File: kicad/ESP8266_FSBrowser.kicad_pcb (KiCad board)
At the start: 2 copper layers, 28 parts, among them P1 POWER, P2 GPIO, P3 SERIAL, SW1 RESET, SW2 AP_ENABLE, SW3 FLASH, U1 ESP-12E, U2 SPX3819M5-L-3-3

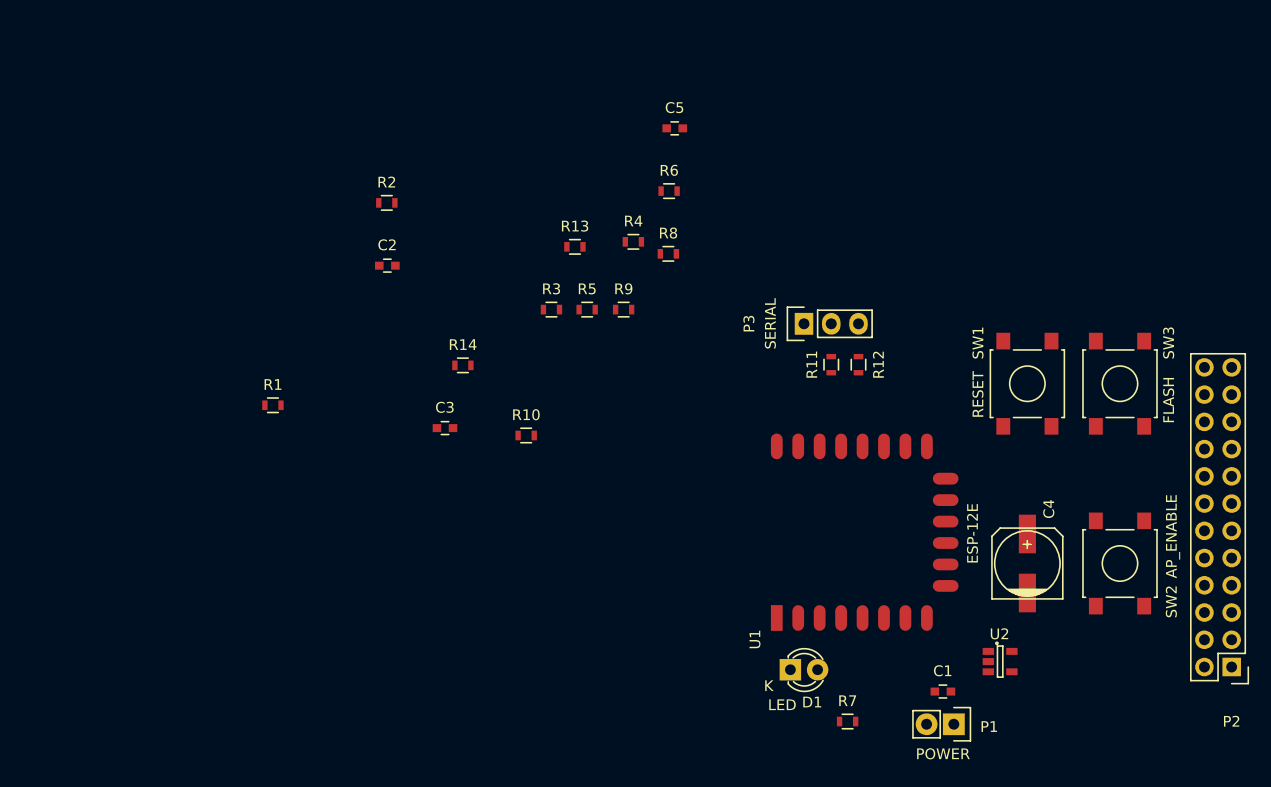
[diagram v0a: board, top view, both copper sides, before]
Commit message: Revert "Play with kicad files"
This reverts commit 04bb3029db1baf8c5355bf4588b1dad35f342a4f.
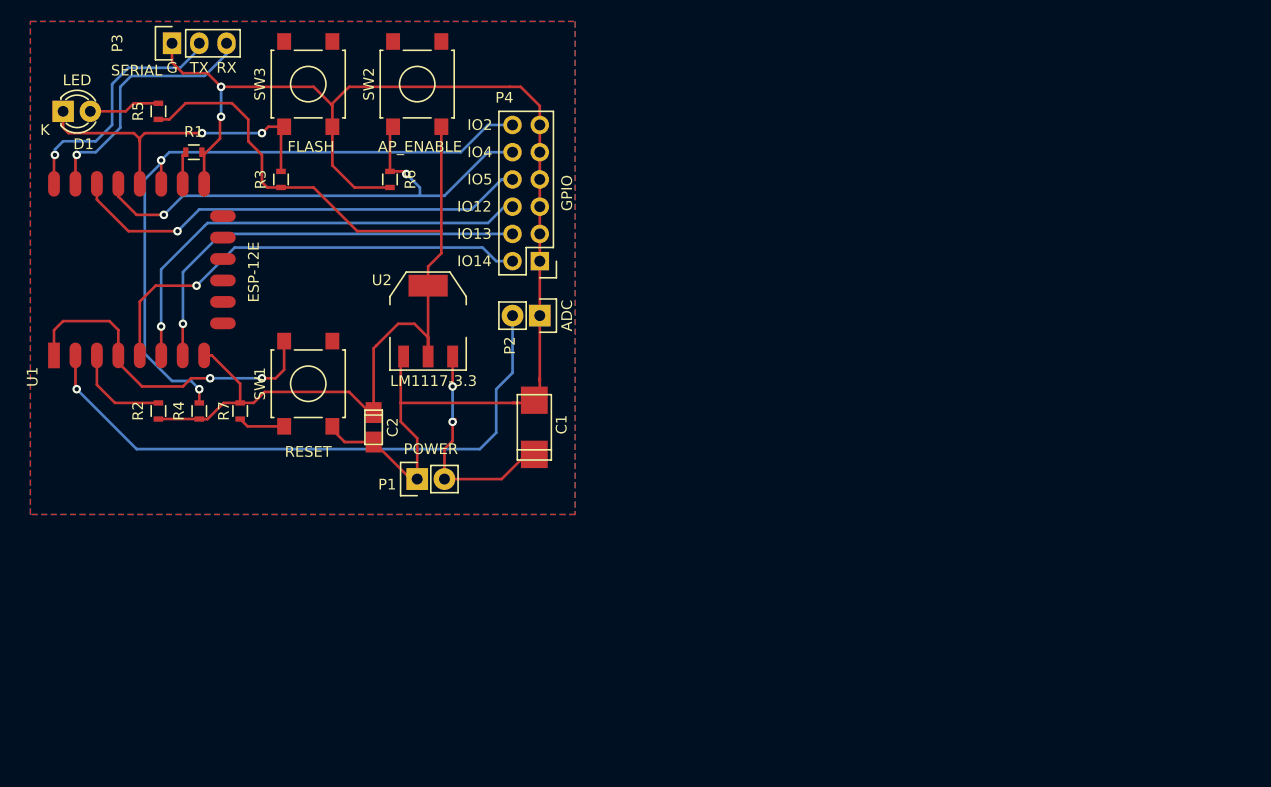
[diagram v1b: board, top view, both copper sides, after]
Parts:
- removed C3, C5: 470p, Capacitors_SMD:C_0603
- removed C4: 100u, Capacitors_SMD:c_elec_6.3x5.8
- removed R10: 0, Resistors_SMD:R_0603
- removed R11, R12: 470, Resistors_SMD:R_0603
- removed R13: 220k(1%), Resistors_SMD:R_0603
- removed R14: 100k(1%), Resistors_SMD:R_0603
- removed R8: 10k, Resistors_SMD:R_0603
- removed R9: 220, Resistors_SMD:R_0603
- added P4: GPIO, Pin_Headers:Pin_Header_Straight_2x06, F.Cu at (102.9, 55.9)
- C1: value 1u -> 10u; footprint Capacitors_SMD:C_0603 -> Capacitors_Tantalum_SMD:TantalC_SizeU_EIA-6032
- C2: value 10u -> 1u; footprint Capacitors_SMD:C_0603 -> Capacitors_Tantalum_SMD:TantalC_SizeS_EIA-3216
- P2: value GPIO -> ADC; footprint Pin_Headers:Pin_Header_Straight_2x12 -> Pin_Headers:Pin_Header_Straight_1x02
- R5: value 470 -> 330
- U2: value SPX3819M5-L-3-3 -> LM1117-3.3; footprint TO_SOT_Packages_SMD:SOT-23-5 -> TO_SOT_Packages_SMD:SOT-223
- moved D1 85.5 mm to (58.4, 41.9)
- moved SW3 80.7 mm to (81.3, 39.4)
- moved SW2 79.3 mm to (91.4, 39.4), turned to 90 degrees
- moved P2 72.4 mm to (102.9, 61.0), turned to 270 degrees
- moved U1 71.7 mm to (57.6, 64.7)
- moved SW1 67.1 mm to (81.3, 67.3), turned to 90 degrees
- moved P3 64.5 mm to (68.6, 35.6)
- moved R7 63.6 mm to (74.9, 69.8), turned to 270 degrees
- moved U2 62.1 mm to (92.5, 61.5)
- moved P1 55.0 mm to (91.4, 76.2), turned to 90 degrees
- moved C1 45.4 mm to (102.4, 71.4), turned to 270 degrees
- moved R5 44.0 mm to (67.3, 41.9), turned to 90 degrees
- moved R4 43.4 mm to (71.1, 69.8), turned to 90 degrees
- moved R2 28.8 mm to (67.3, 69.8), turned to 90 degrees
- moved R3 28.0 mm to (78.7, 48.3), turned to 90 degrees
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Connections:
- net GPIO15 renamed Net-(R1-Pad1)
- C1 pad 1: +5V -> Net-(C1-Pad1)
- D1 pad 1: GPIO16 -> Net-(D1-Pad1)
- P1 pad 2: +5V -> Net-(C1-Pad1)
- P2 pad 2: Net-(P2-Pad2) -> ADC
- R2 pad 1: CH_PD -> +3V3
- R2 pad 2: +3V3 -> Net-(R2-Pad2)
- R3 pad 1: GPIO2 -> +3V3
- R3 pad 2: +3V3 -> Net-(D1-Pad1)
- R4 pad 1: GPIO0 -> +3V3
- R4 pad 2: +3V3 -> GPIO2
- R6 pad 1: GPIO4 -> AP_EN
- R7 pad 1: GPIO16 -> +3V3
- R7 pad 2: Net-(R10-Pad2) -> RST
- SW1 pad 1: GND -> RST
- SW1 pad 2: Net-(R10-Pad2) -> GND
- SW2 pad 1: GPIO4 -> AP_EN
- SW3 pad 1: Net-(R9-Pad1) -> Net-(D1-Pad1)
- U1 pad 18: GPIO0 -> Net-(D1-Pad1)
- U1 pad 19: GPIO4 -> AP_EN
- U1 pad 21: Net-(R12-Pad2) -> Net-(P3-Pad3)
- U1 pad 22: Net-(R11-Pad2) -> Net-(P3-Pad2)
- U1 pad 3: CH_PD -> Net-(R2-Pad2)
- U1 pad 4: GPIO16 -> RST
- U2 pad 1: +5V -> GND
- U2 pad 2: GND -> +3V3
- U2 pad 3: +5V -> Net-(C1-Pad1)
- U2 pad 4: Net-(C5-Pad1) -> +3V3
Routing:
- net GND: track 0.00 -> 124.1 mm, vias 0 -> 2
- net +3V3: track 0.00 -> 99.1 mm
- net GPIO2: track 0.00 -> 62.7 mm, vias 0 -> 2
- net ADC: track 0.00 -> 56.8 mm, vias 0 -> 1
- net AP_EN: track 0.00 -> 49.5 mm, vias 0 -> 2
- net GPIO5: track 0.00 -> 43.4 mm, vias 0 -> 1
- net GPIO12: track 0.00 -> 43.2 mm, vias 0 -> 1
- net GPIO14: track 0.00 -> 42.6 mm, vias 0 -> 1
- net GPIO13: track 0.00 -> 40.0 mm, vias 0 -> 1
- net RST: track 0.00 -> 36.2 mm, vias 0 -> 2
- net Net-(D1-Pad1): track 0.00 -> 31.8 mm, vias 0 -> 2
- net Net-(P3-Pad3): track 0.00 -> 23.9 mm, vias 0 -> 1
- net Net-(P3-Pad2): track 0.00 -> 23.3 mm, vias 0 -> 1
- net Net-(C1-Pad1): track 0.00 -> 21.5 mm, vias 0 -> 2
- net Net-(R2-Pad2): track 0.00 -> 9.18 mm
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- added copper zone on B.Cu, net GND
- added copper zone on F.Cu, net GND
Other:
- board text added: "G"
- board text added: "IO12"
- board text added: "IO13"
- board text added: "IO14"
- board text added: "IO2"
- board text added: "IO4"
- board text added: "IO5"
- board text added: "RX"
- board text added: "TX"

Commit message: Play with kicad files
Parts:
- removed P4: GPIO, Pin_Headers:Pin_Header_Straight_2x06
- added C3: 470p, Capacitors_SMD:C_0603, F.Cu at (94.0, 71.4)
- added C4: 100u, Capacitors_SMD:c_elec_6.3x5.8, F.Cu at (148.3, 84.1)
- added C5: 470p, Capacitors_SMD:C_0603, F.Cu at (115.5, 43.5)
- added R10: 0, Resistors_SMD:R_0603, F.Cu at (101.6, 72.1)
- added R11: 470, Resistors_SMD:R_0603, F.Cu at (130.0, 65.5)
- added R12: 470, Resistors_SMD:R_0603, F.Cu at (132.6, 65.5)
- added R13: 220k(1%), Resistors_SMD:R_0603, F.Cu at (106.1, 54.5)
- added R14: 100k(1%), Resistors_SMD:R_0603, F.Cu at (95.7, 65.6)
- added R8: 10k, Resistors_SMD:R_0603, F.Cu at (114.9, 55.2)
- added R9: 220, Resistors_SMD:R_0603, F.Cu at (110.7, 60.4)
- C1: value 10u -> 1u; footprint Capacitors_Tantalum_SMD:TantalC_SizeU_EIA-6032 -> Capacitors_SMD:C_0603
- C2: value 1u -> 10u; footprint Capacitors_Tantalum_SMD:TantalC_SizeS_EIA-3216 -> Capacitors_SMD:C_0603
- P2: value ADC -> GPIO; footprint Pin_Headers:Pin_Header_Straight_1x02 -> Pin_Headers:Pin_Header_Straight_2x12
- R5: value 330 -> 470
- U2: value LM1117-3.3 -> SPX3819M5-L-3-3; footprint TO_SOT_Packages_SMD:SOT-223 -> TO_SOT_Packages_SMD:SOT-23-5
- moved D1 85.5 mm to (126.2, 94.0)
- moved SW3 80.7 mm to (157.0, 67.3)
- moved SW2 79.3 mm to (157.0, 84.1), turned to 270 degrees
- moved P2 72.4 mm to (167.4, 93.7), turned to 180 degrees
- moved U1 71.7 mm to (125.0, 89.2)
- moved SW1 67.1 mm to (148.3, 67.3), turned to 270 degrees
- moved P3 64.5 mm to (127.5, 61.7)
- moved R7 63.6 mm to (131.6, 98.8), turned to 0 degrees
- moved U2 62.1 mm to (145.8, 93.2)
- moved P1 55.0 mm to (141.5, 99.1), turned to 270 degrees
- moved C1 45.4 mm to (140.5, 96.0), turned to 0 degrees
- moved R5 44.0 mm to (107.3, 60.4), turned to 0 degrees
- moved R4 43.4 mm to (111.6, 54.1), turned to 0 degrees
- moved R2 28.8 mm to (88.6, 50.4), turned to 0 degrees
- moved R3 28.0 mm to (104.0, 60.4), turned to 0 degrees
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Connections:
- net Net-(R1-Pad1) renamed GPIO15
- C1 pad 1: Net-(C1-Pad1) -> +5V
- D1 pad 1: Net-(D1-Pad1) -> GPIO16
- P1 pad 2: Net-(C1-Pad1) -> +5V
- P2 pad 2: ADC -> Net-(P2-Pad2)
- R2 pad 1: +3V3 -> CH_PD
- R2 pad 2: Net-(R2-Pad2) -> +3V3
- R3 pad 1: +3V3 -> GPIO2
- R3 pad 2: Net-(D1-Pad1) -> +3V3
- R4 pad 1: +3V3 -> GPIO0
- R4 pad 2: GPIO2 -> +3V3
- R6 pad 1: AP_EN -> GPIO4
- R7 pad 1: +3V3 -> GPIO16
- R7 pad 2: RST -> Net-(R10-Pad2)
- SW1 pad 1: RST -> GND
- SW1 pad 2: GND -> Net-(R10-Pad2)
- SW2 pad 1: AP_EN -> GPIO4
- SW3 pad 1: Net-(D1-Pad1) -> Net-(R9-Pad1)
- U1 pad 18: Net-(D1-Pad1) -> GPIO0
- U1 pad 19: AP_EN -> GPIO4
- U1 pad 21: Net-(P3-Pad3) -> Net-(R12-Pad2)
- U1 pad 22: Net-(P3-Pad2) -> Net-(R11-Pad2)
- U1 pad 3: Net-(R2-Pad2) -> CH_PD
- U1 pad 4: RST -> GPIO16
- U2 pad 1: GND -> +5V
- U2 pad 2: +3V3 -> GND
- U2 pad 3: Net-(C1-Pad1) -> +5V
- U2 pad 4: +3V3 -> Net-(C5-Pad1)
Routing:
- net GND: track 124.1 -> 0.00 mm, vias 2 -> 0
- net +3V3: track 99.1 -> 0.00 mm
- net GPIO2: track 62.7 -> 0.00 mm, vias 2 -> 0
- net ADC: track 56.8 -> 0.00 mm, vias 1 -> 0
- net AP_EN: track 49.5 -> 0.00 mm, vias 2 -> 0
- net GPIO5: track 43.4 -> 0.00 mm, vias 1 -> 0
- net GPIO12: track 43.2 -> 0.00 mm, vias 1 -> 0
- net GPIO14: track 42.6 -> 0.00 mm, vias 1 -> 0
- net GPIO13: track 40.0 -> 0.00 mm, vias 1 -> 0
- net RST: track 36.2 -> 0.00 mm, vias 2 -> 0
- net Net-(D1-Pad1): track 31.8 -> 0.00 mm, vias 2 -> 0
- net Net-(P3-Pad3): track 23.9 -> 0.00 mm, vias 1 -> 0
- net Net-(P3-Pad2): track 23.3 -> 0.00 mm, vias 1 -> 0
- net Net-(C1-Pad1): track 21.5 -> 0.00 mm, vias 2 -> 0
- net Net-(R2-Pad2): track 9.18 -> 0.00 mm
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- removed copper zone on B.Cu, net GND
- removed copper zone on F.Cu, net GND
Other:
- board text removed: "G"
- board text removed: "IO12"
- board text removed: "IO13"
- board text removed: "IO14"
- board text removed: "IO2"
- board text removed: "IO4"
- board text removed: "IO5"
- board text removed: "RX"
- board text removed: "TX"
